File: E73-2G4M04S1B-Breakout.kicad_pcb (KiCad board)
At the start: 2 copper layers, 22.5 x 86.3 mm, 3 parts, among them J1 Conn_01x20_Male, J2 Conn_01x20_Male, U1 E73-2G4M04S1B

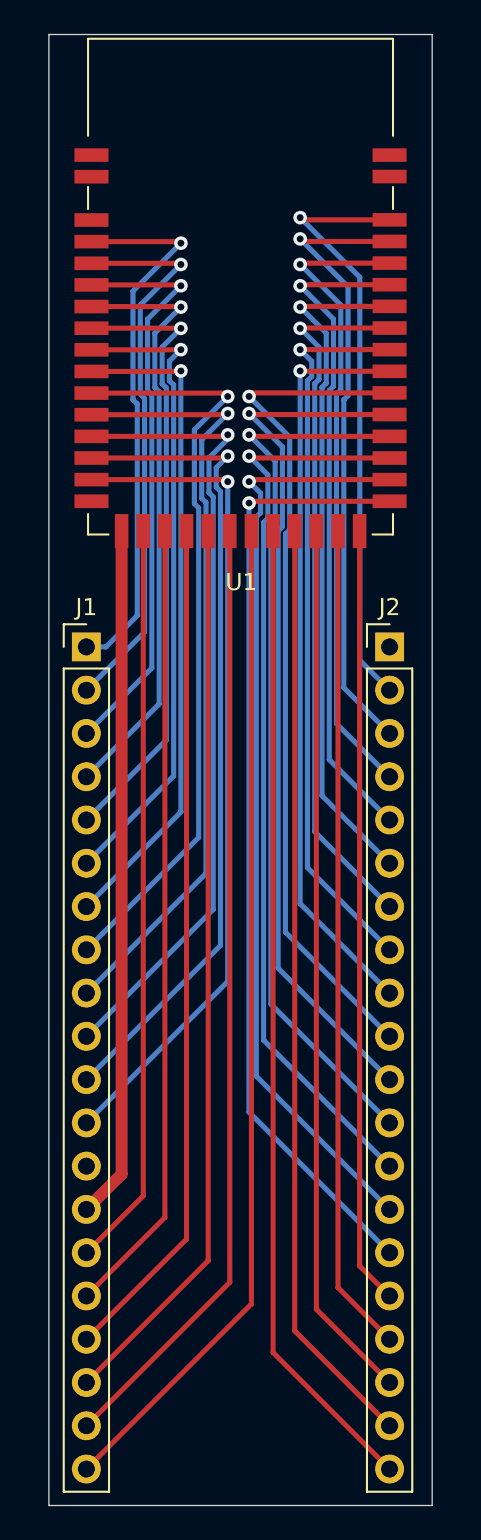
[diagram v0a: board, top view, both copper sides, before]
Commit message: Added copper fill
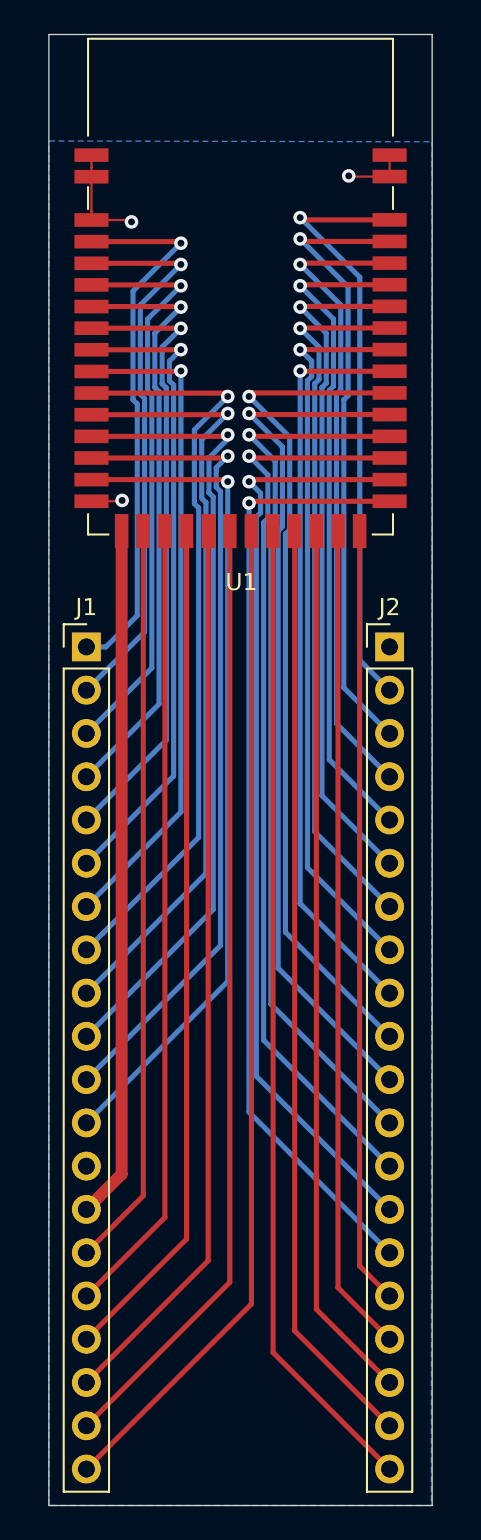
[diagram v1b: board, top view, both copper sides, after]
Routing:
- net GND: track 0.00 -> 11.7 mm, vias 0 -> 3
- added copper zone on B.Cu, net GND
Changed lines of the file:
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@@
     (thickness 1.6)
     (drawings 4)
-    (tracks 224)
+    (tracks 238)
     (zones 0)
     (modules 3)
@@
   )
   (setup
-    (last_trace_width 0.3)
+    (last_trace_width 0.127)
     (user_trace_width 0.3)
     (user_trace_width 0.7)
@@
   (segment (start 145.77 125.65) (end 143.7 127.72) (width 0.7) (layer F.Cu) (net 7))
   (segment (start 145.77 87.9) (end 145.77 125.65) (width 0.7) (layer F.Cu) (net 7))
+  (segment (start 144 69.113) (end 144 67.1) (width 0.127) (layer F.Cu) (net 8))
+  (segment (start 144 69.64) (end 144 69.113) (width 0.127) (layer F.Cu) (net 8))
+  (segment (start 144 66.573) (end 144 65.83) (width 0.127) (layer F.Cu) (net 8))
+  (segment (start 144 67.1) (end 144 66.573) (width 0.127) (layer F.Cu) (net 8))
+  (via (at 146.35 69.75) (size 0.8) (drill 0.4) (layers F.Cu B.Cu) (net 8))
+  (segment (start 146.24 69.64) (end 146.35 69.75) (width 0.127) (layer F.Cu) (net 8))
+  (segment (start 144 69.64) (end 146.24 69.64) (width 0.127) (layer F.Cu) (net 8))
+  (segment (start 161.5 65.83) (end 161.5 67.09) (width 0.127) (layer F.Cu) (net 8))
+  (via (at 159.1 67.05) (size 0.8) (drill 0.4) (layers F.Cu B.Cu) (net 8))
+  (segment (start 159.14 67.09) (end 159.1 67.05) (width 0.127) (layer F.Cu) (net 8))
+  (segment (start 161.5 67.09) (end 159.14 67.09) (width 0.127) (layer F.Cu) (net 8))
+  (via (at 145.8 86.1) (size 0.8) (drill 0.4) (layers F.Cu B.Cu) (net 8))
+  (segment (start 145.75 86.15) (end 145.8 86.1) (width 0.127) (layer F.Cu) (net 8))
+  (segment (start 144 86.15) (end 145.75 86.15) (width 0.127) (layer F.Cu) (net 8))
   (via (at 152 85) (size 0.8) (drill 0.4) (layers F.Cu B.Cu) (net 9))
   (segment (start 151.88 84.88) (end 152 85) (width 0.3) (layer F.Cu) (net 9))
@@
   (segment (start 154.66 136.12) (end 161.5 142.96) (width 0.3) (layer F.Cu) (net 40))
   (segment (start 154.66 87.9) (end 154.66 136.12) (width 0.3) (layer F.Cu) (net 40))
+  (zone (net 0) (net_name "") (layer B.Cu) (hatch edge 0.508)
+    (connect_pads (clearance 0.508))
+    (min_thickness 0.254)
+    (keepout (tracks not_allowed) (vias not_allowed) (copperpour not_allowed))
+    (fill (arc_segments 32) (thermal_gap 0.508) (thermal_bridge_width 0.508))
+    (polygon
+      (pts
+        (xy 164 65) (xy 141.5 65) (xy 141.5 58.75) (xy 164 58.75)
+      )
+    )
+  )
+  (zone (net 8) (net_name GND) (layer B.Cu) (hatch edge 0.508)
+    (connect_pads (clearance 0.508))
+    (min_thickness 0.254)
+    (fill yes (arc_segments 32) (thermal_gap 0.508) (thermal_bridge_width 0.508))
+    (polygon
+      (pts
+        (xy 164 65.05) (xy 163.95 145.1) (xy 141.5 145.1) (xy 141.5 65)
+      )
+    )
+  )
 )

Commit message: Added pin names
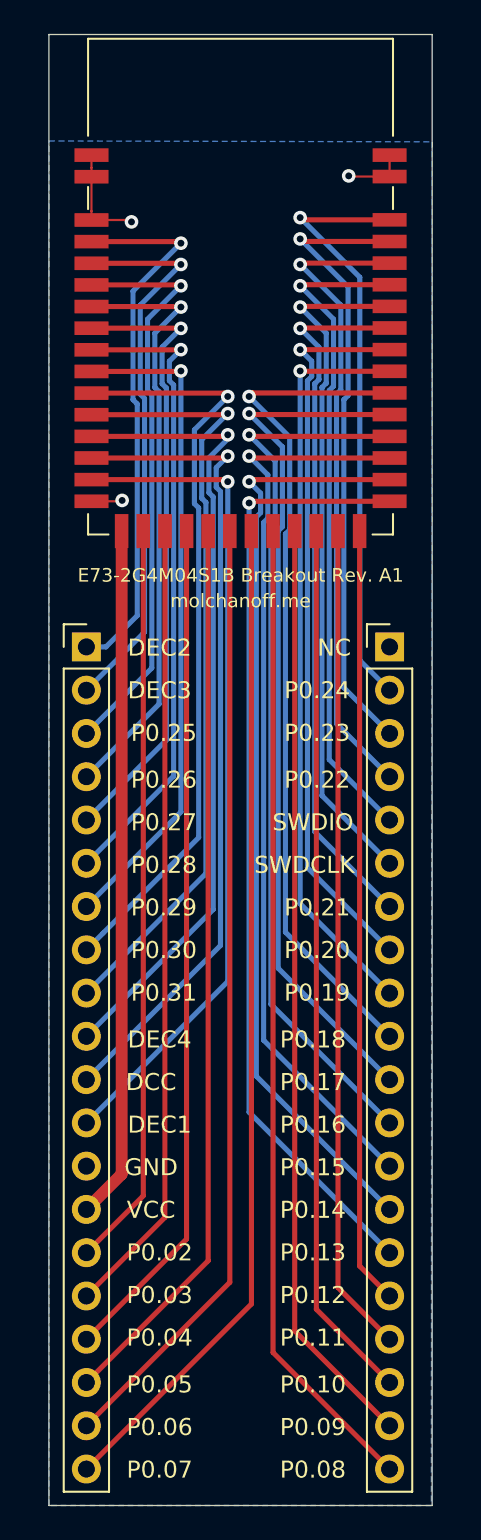
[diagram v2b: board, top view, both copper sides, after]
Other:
- board text added: "DCC"
- board text added: "DEC1"
- board text added: "DEC2"
- board text added: "DEC3"
- board text added: "DEC4"
- board text added: "E73-2G4M04S1B Breakout Rev. A1"
- board text added: "GND"
- board text added: "NC"
- board text added: "P0.02"
- board text added: "P0.03"
- board text added: "P0.04"
- board text added: "P0.05"
- board text added: "P0.06"
- board text added: "P0.07"
- board text added: "P0.08"
- board text added: "P0.09"
- board text added: "P0.10"
- board text added: "P0.11"
- board text added: "P0.12"
- board text added: "P0.13"
- board text added: "P0.14"
- board text added: "P0.15"
- board text added: "P0.16"
- board text added: "P0.17"
- board text added: "P0.18"
- board text added: "P0.19"
- board text added: "P0.20"
- board text added: "P0.21"
- board text added: "P0.22"
- board text added: "P0.23"
- board text added: "P0.24"
- board text added: "P0.25"
- board text added: "P0.26"
- board text added: "P0.27"
- board text added: "P0.28"
- board text added: "P0.29"
- board text added: "P0.30"
- board text added: "P0.31"
- board text added: "SWDCLK"
- board text added: "SWDIO"
- board text added: "VCC"
- board text added: "molchanoff.me"
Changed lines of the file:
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@@
   (general
     (thickness 1.6)
-    (drawings 4)
+    (drawings 46)
     (tracks 238)
     (zones 0)
@@
   )
   (layers
-    (0 F.Cu signal)
-    (31 B.Cu signal)
+    (0 F.Cu signal hide)
+    (31 B.Cu signal hide)
     (32 B.Adhes user)
     (33 F.Adhes user)
@@
   (module Ebyte:E73-2G4M04S1B (layer F.Cu)
     (at 152.8 73.9)
-    (fp_text reference U1 (at 0 17) (layer F.SilkS)
+    (fp_text reference U1 (at 0 17) (layer F.SilkS) hide
       (effects (font (size 1 1) (thickness 0.15)))
     )
@@
     (descr "Through hole straight pin header, 1x20, 2.54mm pitch, single row")
     (tags "Through hole pin header THT 1x20 2.54mm single row")
-    (fp_text reference J1 (at 0 -2.33) (layer F.SilkS)
+    (fp_text reference J1 (at 0 -2.33) (layer F.SilkS) hide
       (effects (font (size 1 1) (thickness 0.15)))
     )
@@
     (descr "Through hole straight pin header, 1x20, 2.54mm pitch, single row")
     (tags "Through hole pin header THT 1x20 2.54mm single row")
-    (fp_text reference J2 (at 0 -2.33) (layer F.SilkS)
+    (fp_text reference J2 (at 0 -2.33) (layer F.SilkS) hide
       (effects (font (size 1 1) (thickness 0.15)))
     )
@@
     )
   )
+  (gr_text molchanoff.me (at 152.75 92) (layer F.SilkS)
+    (effects (font (size 0.8 0.8) (thickness 0.2)))
+  )
+  (gr_text "E73-2G4M04S1B Breakout Rev. A1" (at 152.75 90.5) (layer F.SilkS)
+    (effects (font (size 0.8 0.8) (thickness 0.175)))
+  )
+  (gr_text P0.24 (at 157.25 97.25) (layer F.SilkS)
+    (effects (font (size 1 1) (thickness 0.25)))
+  )
+  (gr_text P0.17 (at 157 120.25) (layer F.SilkS)
+    (effects (font (size 1 1) (thickness 0.25)))
+  )
+  (gr_text P0.10 (at 157 138) (layer F.SilkS)
+    (effects (font (size 1 1) (thickness 0.25)))
+  )
+  (gr_text P0.12 (at 157 132.75) (layer F.SilkS)
+    (effects (font (size 1 1) (thickness 0.25)))
+  )
+  (gr_text P0.23 (at 157.25 99.75) (layer F.SilkS)
+    (effects (font (size 1 1) (thickness 0.25)))
+  )
+  (gr_text P0.08 (at 157 143) (layer F.SilkS)
+    (effects (font (size 1 1) (thickness 0.25)))
+  )
+  (gr_text P0.11 (at 157 135.25) (layer F.SilkS)
+    (effects (font (size 1 1) (thickness 0.25)))
+  )
+  (gr_text NC (at 158.25 94.75) (layer F.SilkS)
+    (effects (font (size 1 1) (thickness 0.25)))
+  )
+  (gr_text P0.09 (at 157 140.5) (layer F.SilkS)
+    (effects (font (size 1 1) (thickness 0.25)))
+  )
+  (gr_text P0.15 (at 157 125.25) (layer F.SilkS)
+    (effects (font (size 1 1) (thickness 0.25)))
+  )
+  (gr_text SWDCLK (at 156.5 107.5) (layer F.SilkS)
+    (effects (font (size 1 1) (thickness 0.25)))
+  )
+  (gr_text P0.16 (at 157 122.75) (layer F.SilkS)
+    (effects (font (size 1 1) (thickness 0.25)))
+  )
+  (gr_text P0.18 (at 157 117.75) (layer F.SilkS)
+    (effects (font (size 1 1) (thickness 0.25)))
+  )
+  (gr_text P0.22 (at 157.25 102.5) (layer F.SilkS)
+    (effects (font (size 1 1) (thickness 0.25)))
+  )
+  (gr_text SWDIO (at 157 105) (layer F.SilkS)
+    (effects (font (size 1 1) (thickness 0.25)))
+  )
+  (gr_text P0.14 (at 157 127.75) (layer F.SilkS)
+    (effects (font (size 1 1) (thickness 0.25)))
+  )
+  (gr_text P0.13 (at 157 130.25) (layer F.SilkS)
+    (effects (font (size 1 1) (thickness 0.25)))
+  )
+  (gr_text P0.19 (at 157.25 115) (layer F.SilkS)
+    (effects (font (size 1 1) (thickness 0.25)))
+  )
+  (gr_text P0.20 (at 157.25 112.5) (layer F.SilkS)
+    (effects (font (size 1 1) (thickness 0.25)))
+  )
+  (gr_text P0.21 (at 157.25 110) (layer F.SilkS)
+    (effects (font (size 1 1) (thickness 0.25)))
+  )
+  (gr_text P0.07 (at 148 143) (layer F.SilkS)
+    (effects (font (size 1 1) (thickness 0.25)))
+  )
+  (gr_text P0.06 (at 148 140.5) (layer F.SilkS)
+    (effects (font (size 1 1) (thickness 0.25)))
+  )
+  (gr_text P0.05 (at 148 138) (layer F.SilkS)
+    (effects (font (size 1 1) (thickness 0.25)))
+  )
+  (gr_text P0.04 (at 148 135.25) (layer F.SilkS)
+    (effects (font (size 1 1) (thickness 0.25)))
+  )
+  (gr_text P0.03 (at 148 132.75) (layer F.SilkS)
+    (effects (font (size 1 1) (thickness 0.25)))
+  )
+  (gr_text P0.02 (at 148 130.25) (layer F.SilkS)
+    (effects (font (size 1 1) (thickness 0.25)))
+  )
+  (gr_text VCC (at 147.5 127.75) (layer F.SilkS)
+    (effects (font (size 1 1) (thickness 0.25)))
+  )
+  (gr_text GND (at 147.5 125.25) (layer F.SilkS)
+    (effects (font (size 1 1) (thickness 0.25)))
+  )
+  (gr_text DEC1 (at 148 122.75) (layer F.SilkS)
+    (effects (font (size 1 1) (thickness 0.25)))
+  )
+  (gr_text DCC (at 147.5 120.25) (layer F.SilkS)
+    (effects (font (size 1 1) (thickness 0.25)))
+  )
+  (gr_text DEC4 (at 148 117.75) (layer F.SilkS)
+    (effects (font (size 1 1) (thickness 0.25)))
+  )
+  (gr_text P0.31 (at 148.25 115) (layer F.SilkS)
+    (effects (font (size 1 1) (thickness 0.25)))
+  )
+  (gr_text P0.30 (at 148.25 112.5) (layer F.SilkS)
+    (effects (font (size 1 1) (thickness 0.25)))
+  )
+  (gr_text P0.29 (at 148.25 110) (layer F.SilkS)
+    (effects (font (size 1 1) (thickness 0.25)))
+  )
+  (gr_text P0.28 (at 148.25 107.5) (layer F.SilkS)
+    (effects (font (size 1 1) (thickness 0.25)))
+  )
+  (gr_text P0.27 (at 148.25 105) (layer F.SilkS)
+    (effects (font (size 1 1) (thickness 0.25)))
+  )
+  (gr_text DEC2 (at 148 94.75) (layer F.SilkS)
+    (effects (font (size 1 1) (thickness 0.25)))
+  )
+  (gr_text DEC3 (at 148 97.25) (layer F.SilkS)
+    (effects (font (size 1 1) (thickness 0.25)))
+  )
+  (gr_text P0.26 (at 148.25 102.5) (layer F.SilkS)
+    (effects (font (size 1 1) (thickness 0.25)))
+  )
+  (gr_text P0.25 (at 148.25 99.75) (layer F.SilkS)
+    (effects (font (size 1 1) (thickness 0.25)))
+  )
   (gr_line (start 141.5 58.75) (end 141.5 145.1) (layer Edge.Cuts) (width 0.05))
